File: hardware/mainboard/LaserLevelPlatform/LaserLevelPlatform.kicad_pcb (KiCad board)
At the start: 2 copper layers, 100 x 40 mm, 45 parts, among them J1 Conn_01x04_Male, J2 Conn_01x04_Male, J3 Conn_02x04_Odd_Even, J4 Conn_01x02_Male, J5 Conn_01x02_Female, J6 Conn_01x02_Male, J7 Conn_01x02_Male, U1 Lolin32, U2 DCDC

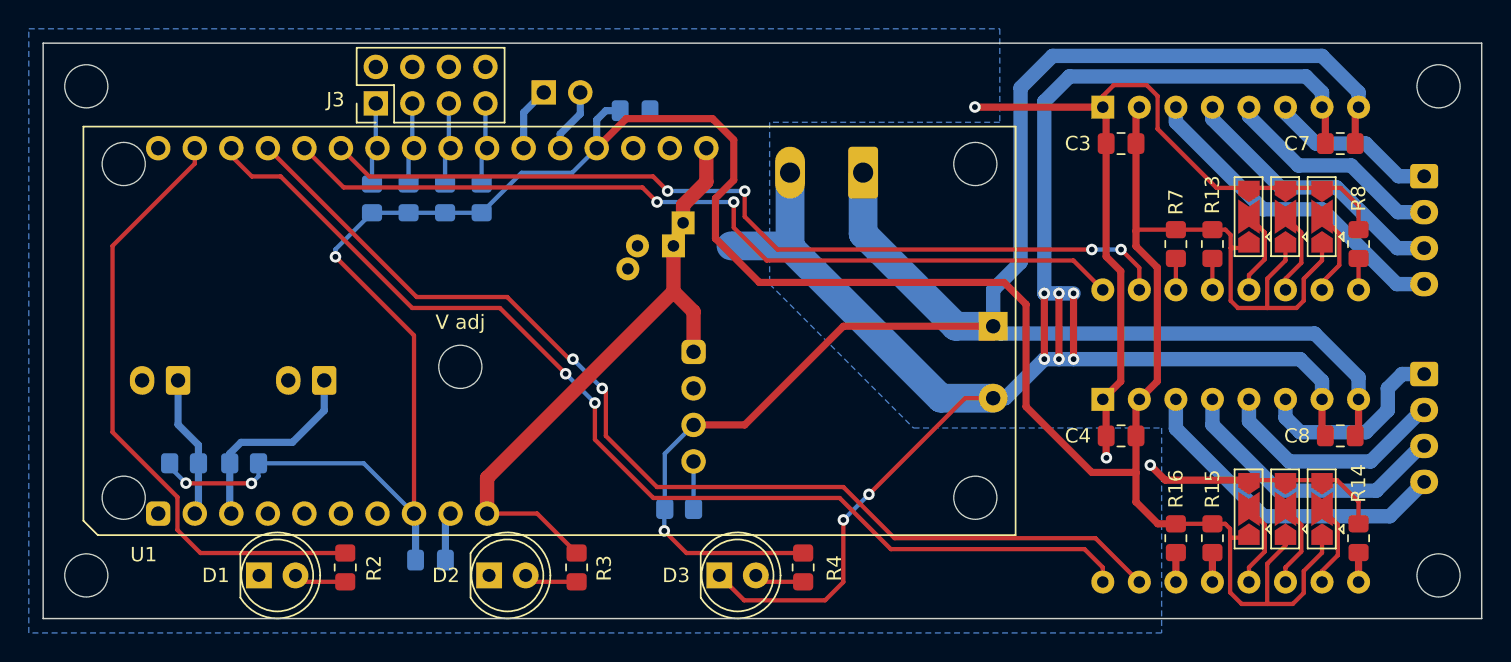
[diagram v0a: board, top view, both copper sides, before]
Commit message: Add jumper on +5V line
Add a jumper to disconnect +5V power line from DC-DC converter from the
main CPU board. This is needed for safe connection of a USB power
together with a +12V input. Also added a bridge in parallel to it for
the permanent connection.
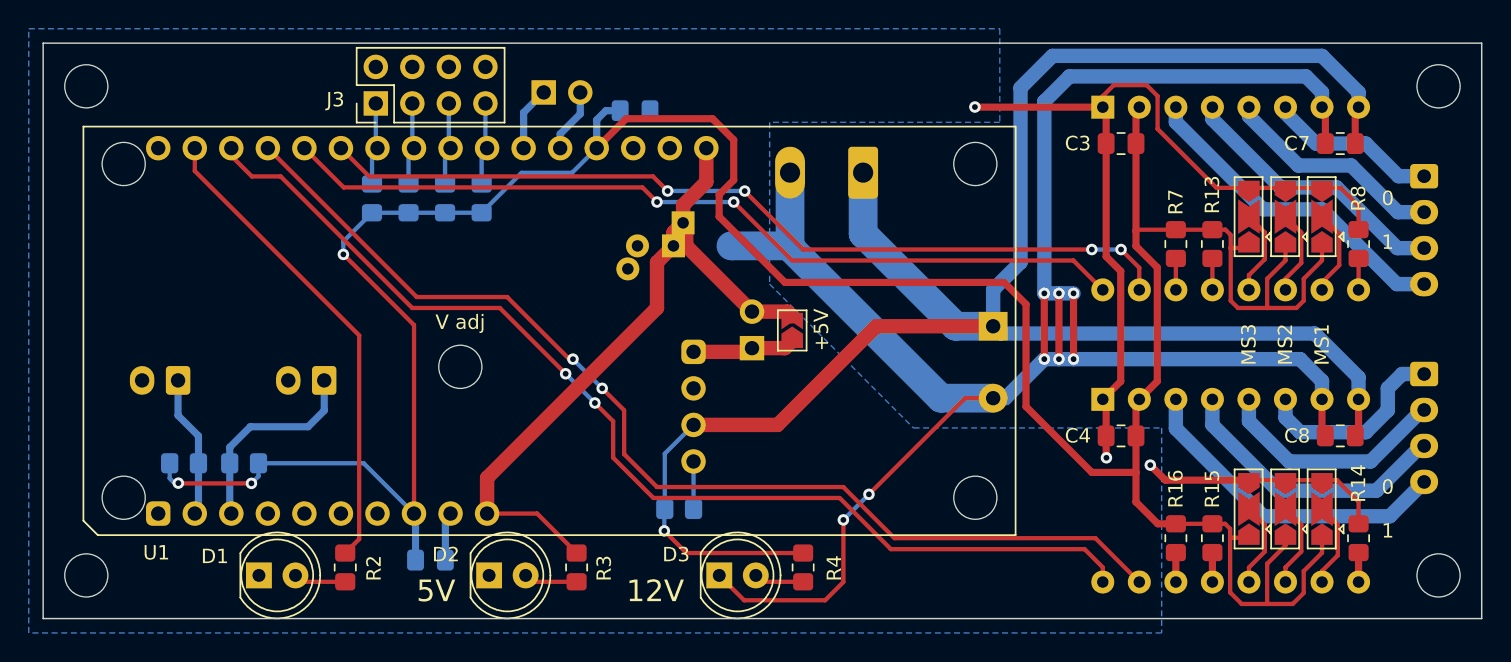
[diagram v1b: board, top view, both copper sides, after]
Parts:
- added J8: Conn_01x02_Male, Connector_PinHeader_2.54mm:PinHeader_1x02_P2.54mm_Vertical, B.Cu at (149.3, 81.2)
- added JP7: Jumper_2_Bridged, Jumper:SolderJumper-2_P1.3mm_Open_TrianglePad1.0x1.5mm, F.Cu at (152.1, 80.0)
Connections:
- net Net-(A1-Pad10) renamed /MS1_1
- net Net-(A1-Pad11) renamed /MS2_1
- net Net-(A1-Pad12) renamed /MS3_1
- net Net-(A2-Pad10) renamed /MS1_2
- net Net-(A2-Pad11) renamed /MS2_2
- net Net-(A2-Pad12) renamed /MS3_2
- U2 pad 1: +5V -> /5V_out
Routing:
- net /fault: track 43.1 -> 33.3 mm
- net +5V: track 42.0 -> 51.0 mm
- net /5V_out: track 0.00 -> 7.17 mm
- net +3.3V: track 212.1 -> 210.9 mm
- net /step1: track 61.5 -> 60.5 mm
- net /dir1: track 60.6 -> 59.6 mm
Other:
- board text added: "+5V"
- board text added: "0"
- board text added: "1"
- board text added: "12V"
- board text added: "5V"
- board text added: "MS1"
- board text added: "MS2"
- board text added: "MS3"
